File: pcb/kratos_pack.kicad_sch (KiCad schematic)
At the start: 96 parts, among them J1 USB_C_Receptacle_USB2.0, J2 PROG_CONN_STM_6p, J3 DBG_UART, J4 BAT_MID+NTC, J5 BAT_7.4V, J6 BAT_0V, J7 OUT+, J8 OUT-, Q1 AON7403, Q2 AON7414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

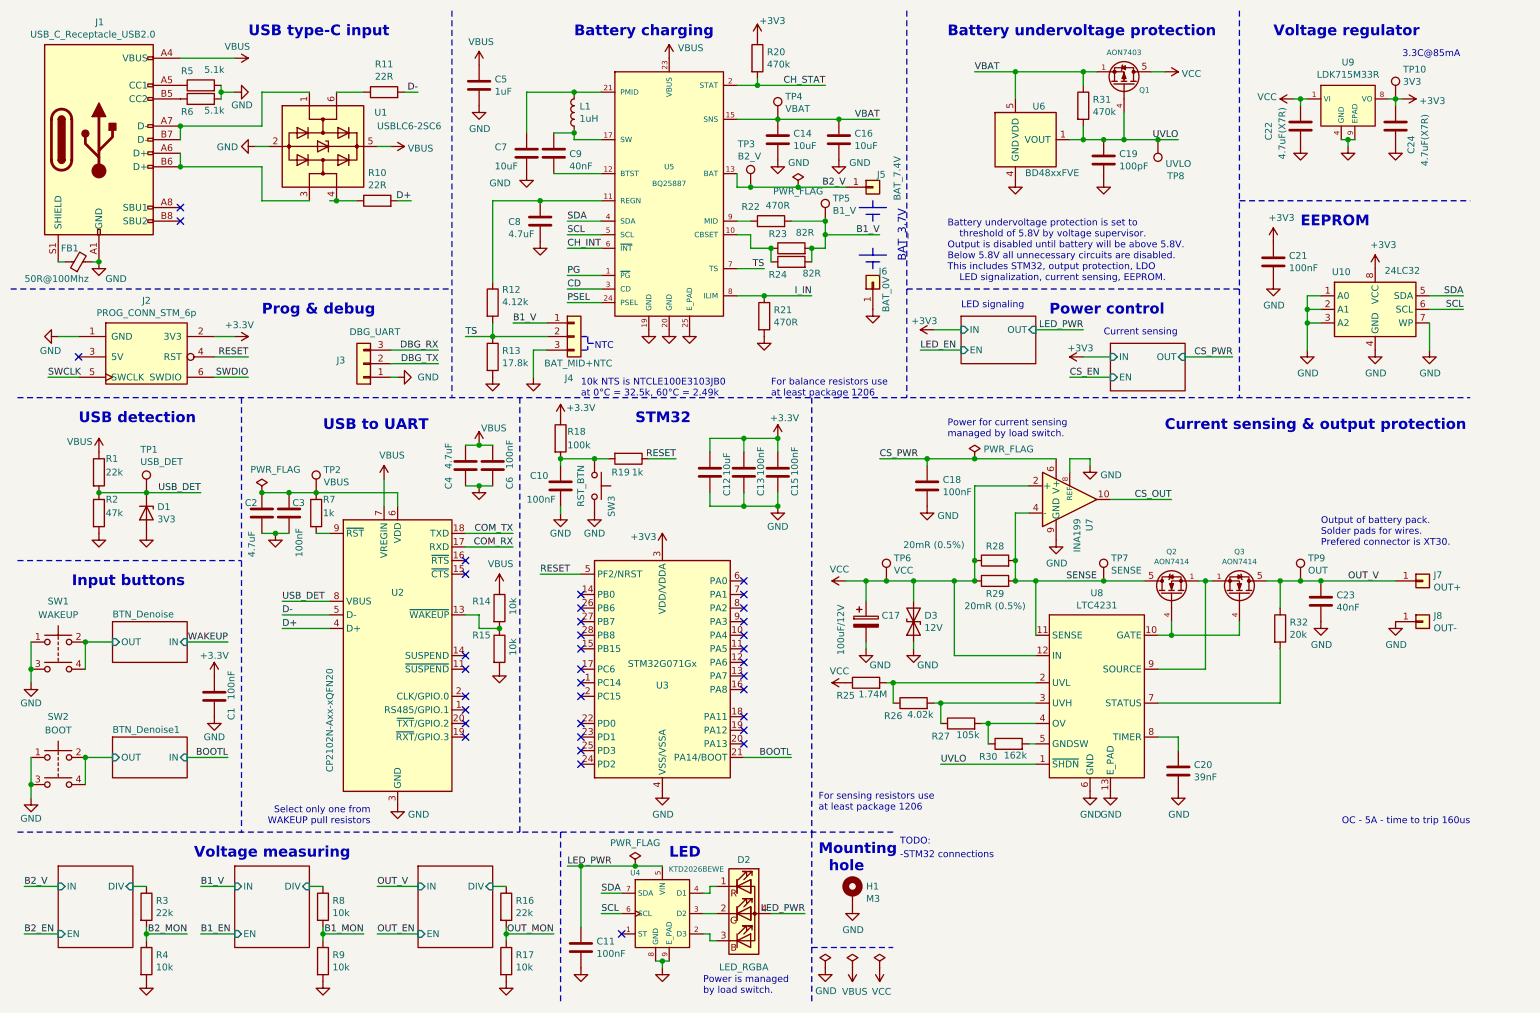
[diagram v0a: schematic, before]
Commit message: Schema: bom optimization
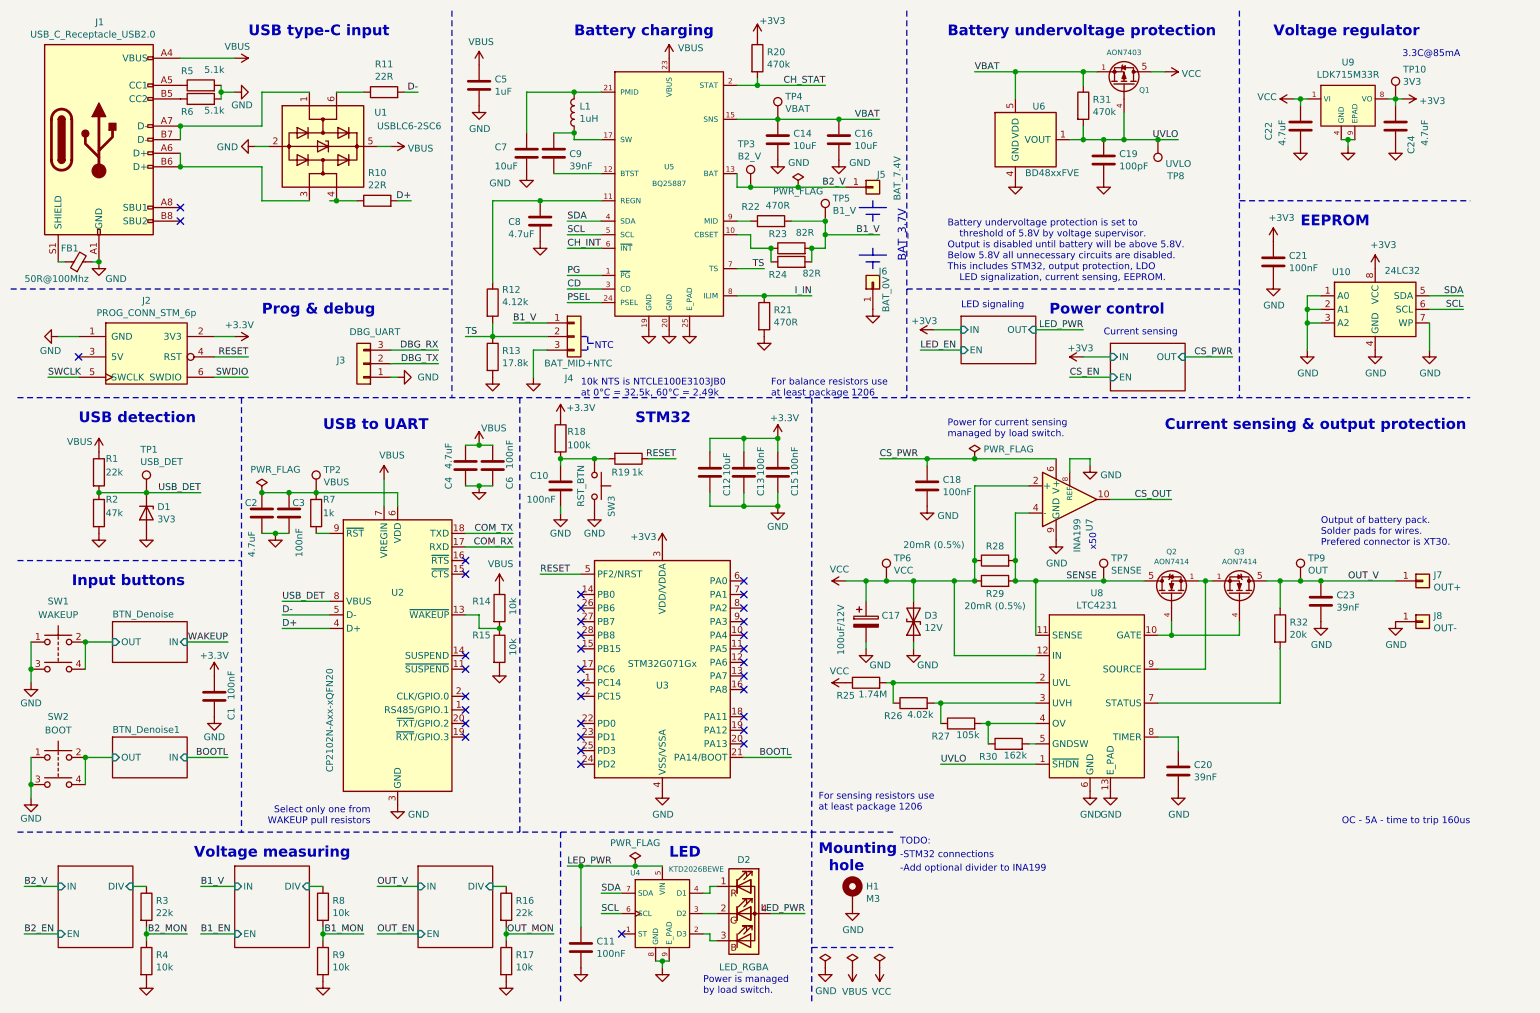
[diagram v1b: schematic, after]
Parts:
- C22, C24: value 4.7uF(X7R) -> 4.7uF
- C23, C9: value 40nF -> 39nF
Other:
- note added: "-Add optional divider to INA199"
- note added: "x50"
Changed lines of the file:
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@@
   (junction (at 261.62 36.83) (diameter 1.016) (color 0 0 0 0))
   (junction (at 270.51 29.21) (diameter 1.016) (color 0 0 0 0))
-  (no_connect (at 148.59 119.38))
-  (no_connect (at 148.59 144.78))
-  (no_connect (at 118.11 153.67))
-  (no_connect (at 118.11 148.59))
-  (no_connect (at 96.52 135.89))
-  (no_connect (at 118.11 135.89))
+  (no_connect (at 96.52 148.59))
+  (no_connect (at 118.11 121.92))
+  (no_connect (at 148.59 139.7))
   (no_connect (at 118.11 151.13))
+  (no_connect (at 96.52 133.35))
+  (no_connect (at 43.18 49.53))
+  (no_connect (at 148.59 137.16))
+  (no_connect (at 118.11 127))
+  (no_connect (at 148.59 147.32))
+  (no_connect (at 148.59 119.38))
   (no_connect (at 96.52 118.11))
-  (no_connect (at 118.11 132.08))
-  (no_connect (at 148.59 121.92))
-  (no_connect (at 118.11 129.54))
-  (no_connect (at 43.18 52.07))
-  (no_connect (at 24.13 77.47))
+  (no_connect (at 118.11 138.43))
+  (no_connect (at 118.11 148.59))
   (no_connect (at 96.52 143.51))
-  (no_connect (at 118.11 127))
-  (no_connect (at 118.11 146.05))
-  (no_connect (at 96.52 146.05))
+  (no_connect (at 148.59 121.92))
   (no_connect (at 148.59 132.08))
-  (no_connect (at 96.52 140.97))
-  (no_connect (at 148.59 147.32))
-  (no_connect (at 148.59 137.16))
-  (no_connect (at 148.59 139.7))
-  (no_connect (at 43.18 49.53))
-  (no_connect (at 148.59 124.46))
-  (no_connect (at 148.59 129.54))
-  (no_connect (at 118.11 121.92))
+  (no_connect (at 118.11 135.89))
+  (no_connect (at 96.52 146.05))
   (no_connect (at 148.59 134.62))
-  (no_connect (at 118.11 138.43))
+  (no_connect (at 148.59 144.78))
+  (no_connect (at 43.18 52.07))
+  (no_connect (at 96.52 115.57))
+  (no_connect (at 148.59 124.46))
   (no_connect (at 118.11 124.46))
-  (no_connect (at 148.59 127))
+  (no_connect (at 96.52 140.97))
   (no_connect (at 125.73 185.42))
-  (no_connect (at 96.52 115.57))
-  (no_connect (at 96.52 133.35))
-  (no_connect (at 118.11 140.97))
+  (no_connect (at 148.59 127))
+  (no_connect (at 118.11 129.54))
+  (no_connect (at 118.11 146.05))
+  (no_connect (at 24.13 77.47))
+  (no_connect (at 118.11 153.67))
   (no_connect (at 148.59 149.86))
-  (no_connect (at 96.52 148.59))
+  (no_connect (at 118.11 140.97))
+  (no_connect (at 96.52 135.89))
+  (no_connect (at 148.59 129.54))
+  (no_connect (at 118.11 132.08))
   (wire (pts (xy 13.97 176.53) (xy 20.32 176.53))
     (stroke (width 0) (type solid) (color 0 0 0 0))
@@
     (effects (font (size 1.27 1.27)) (justify left bottom))
   )
+  (text "-Add optional divider to INA199\n" (at 177.8 173.99 0)
+    (effects (font (size 1.27 1.27)) (justify left bottom))
+  )
   (text "BAT_3.7V" (at 179.07 59.69 90)
     (effects (font (size 1.5 1.5)) (justify left bottom))
@@
     (effects (font (size 2 2) (thickness 0.4) bold) (justify left bottom))
   )
+  (text "x50" (at 214.63 110.49 270)
+    (effects (font (size 1.27 1.27)) (justify right bottom))
+  )
   (text "Current sensing" (at 215.9 73.66 0)
     (effects (font (size 1.27 1.27)) (justify left bottom))
@@
   (symbol (lib_id "power:GND") (at 213.36 97.79 0) (unit 1)
     (in_bom yes) (on_board yes)
-    (property "Reference" "#PWR?" (id 0) (at 213.36 104.14 0)
+    (property "Reference" "#PWR0104" (id 0) (at 213.36 104.14 0)
       (effects (font (size 1.27 1.27)) hide)
     )
@@
       (effects (font (size 1.27 1.27)) (justify right))
     )
-    (property "Value" "40nF" (id 1) (at 115.951 41.789 0)
+    (property "Value" "39nF" (id 1) (at 115.951 41.789 0)
       (effects (font (size 1.27 1.27)) (justify right))
     )
@@
       (effects (font (size 1.27 1.27)) (justify left))
     )
-    (property "Value" "4.7uF(X7R)" (id 1) (at 249.301 40.519 90)
+    (property "Value" "4.7uF" (id 1) (at 249.301 37.979 90)
       (effects (font (size 1.27 1.27)) (justify left))
     )
@@
       (effects (font (size 1.27 1.27)) (justify left))
     )
-    (property "Value" "40nF" (id 1) (at 259.461 124.339 0)
+    (property "Value" "39nF" (id 1) (at 259.461 124.339 0)
       (effects (font (size 1.27 1.27)) (justify left))
     )
@@
       (effects (font (size 1.27 1.27)) (justify left))
     )
-    (property "Value" "4.7uF(X7R)" (id 1) (at 275.971 41.789 90)
+    (property "Value" "4.7uF" (id 1) (at 275.971 37.979 90)
       (effects (font (size 1.27 1.27)) (justify left))
     )
@@
     )
     (path "/ecc98303-85ee-40d3-ae87-d94fde20936b"
-      (reference "#PWR?") (unit 1) (value "GND") (footprint "")
+      (reference "#PWR0104") (unit 1) (value "GND") (footprint "")
     )
     (path "/d0d7f179-7f1f-4e2e-b24a-e40d8cea9459"
@@
     )
     (path "/a694cf57-5fc3-42a5-ba36-e20dd2395bd3"
-      (reference "C9") (unit 1) (value "40nF") (footprint "Capacitor_SMD:C_0603_1608Metric")
+      (reference "C9") (unit 1) (value "39nF") (footprint "Capacitor_SMD:C_0603_1608Metric")
     )
     (path "/4882b81f-66f4-4329-b7e2-48e3fe472f6d"
@@
     )
     (path "/10694819-271b-4fa5-ba61-ba7c078c1caf"
-      (reference "C22") (unit 1) (value "4.7uF(X7R)") (footprint "Capacitor_SMD:C_0603_1608Metric")
+      (reference "C22") (unit 1) (value "4.7uF") (footprint "Capacitor_SMD:C_0603_1608Metric")
     )
     (path "/bf7e2eb7-9983-4bef-ae6c-e76472d6cf02"
-      (reference "C23") (unit 1) (value "40nF") (footprint "Capacitor_SMD:C_0603_1608Metric")
+      (reference "C23") (unit 1) (value "39nF") (footprint "Capacitor_SMD:C_0603_1608Metric")
     )
     (path "/deeb4730-0fa2-42da-95d5-a11c25b6e003"
-      (reference "C24") (unit 1) (value "4.7uF(X7R)") (footprint "Capacitor_SMD:C_0603_1608Metric")
+      (reference "C24") (unit 1) (value "4.7uF") (footprint "Capacitor_SMD:C_0603_1608Metric")
     )
     (path "/9ed7c76f-3ba4-4c76-9e97-74ddd55ed5cd"

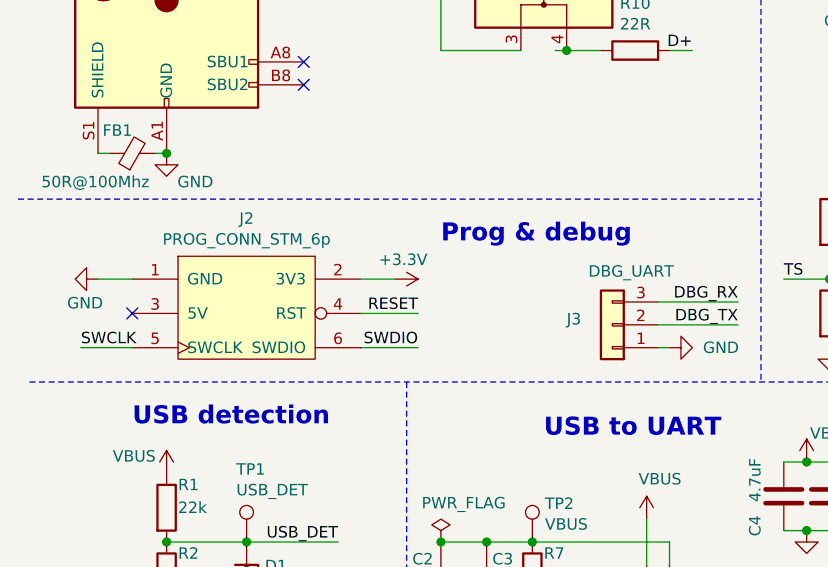
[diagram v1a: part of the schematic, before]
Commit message: Schema: update footprint 3-pin connectors, project cleanup, add gitignore
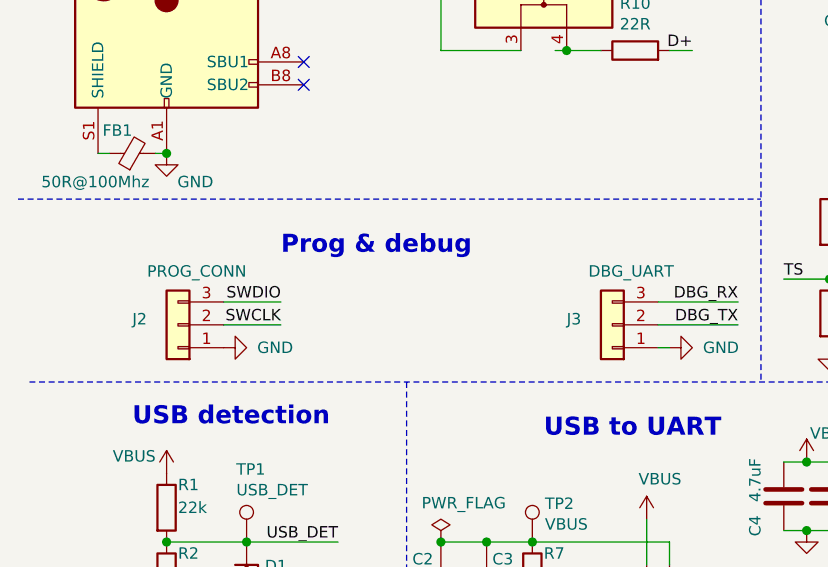
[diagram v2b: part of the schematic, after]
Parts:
- removed J2: PROG_CONN_STM_6p, Connector_PinHeader_1.27mm:PinHeader_2x03_P1.27mm_Vertical, symbol TCY_connectors:PROG_CONN_STM_6p
- added J2: PROG_CONN, TCY_connectors:Amphenol_10114828-11103LF_1x03_P1.25mm_Vertical, symbol Connector_Generic:Conn_01x03
- H1: footprint (none) -> MountingHole:MountingHole_3.2mm_M3_Pad_Via
- J3: footprint Connector_PinHeader_1.27mm:PinHeader_1x03_P1.27mm_Vertical -> TCY_connectors:Amphenol_10114828-11103LF_1x03_P1.25mm_Vertical
- J4: footprint (none) -> TCY_connectors:Amphenol_10114828-11103LF_1x03_P1.25mm_Vertical
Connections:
- net GND: now also J2.1 (Pin_1)
- net SWCLK: now also J2.2 (Pin_2)
- net SWDIO: now also J2.3 (Pin_3)
- no-connect marks 36 -> 35

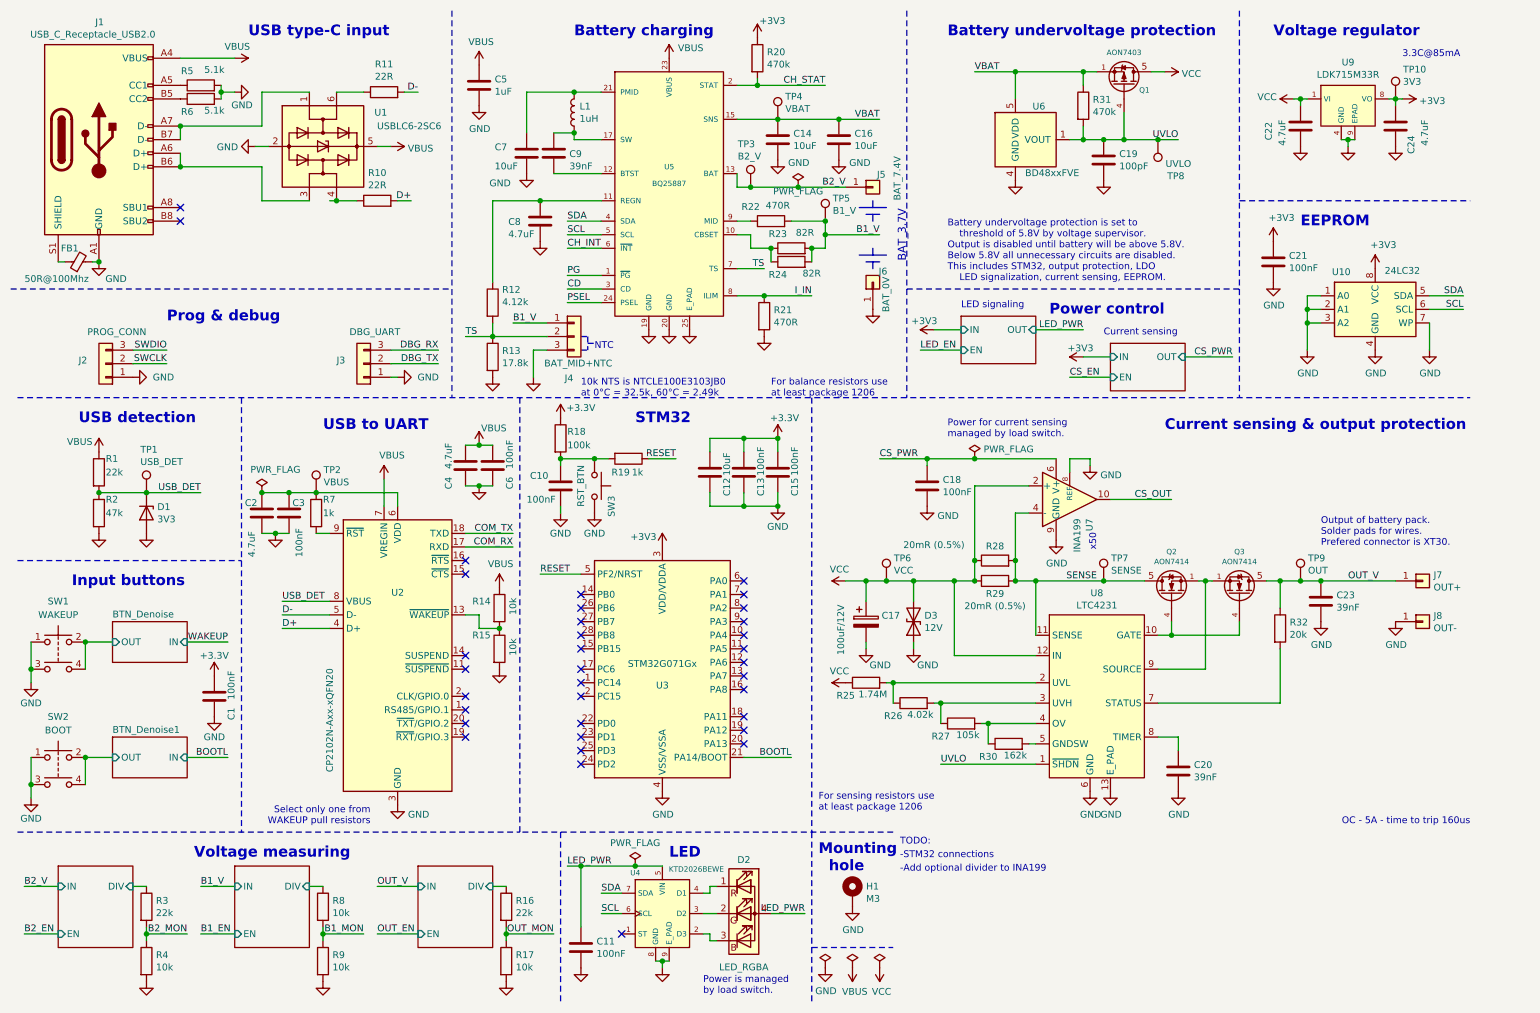
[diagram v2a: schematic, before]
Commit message: Schema: Remove unnecessary test points (switches) and filtering capacitors (STM, CP2102)
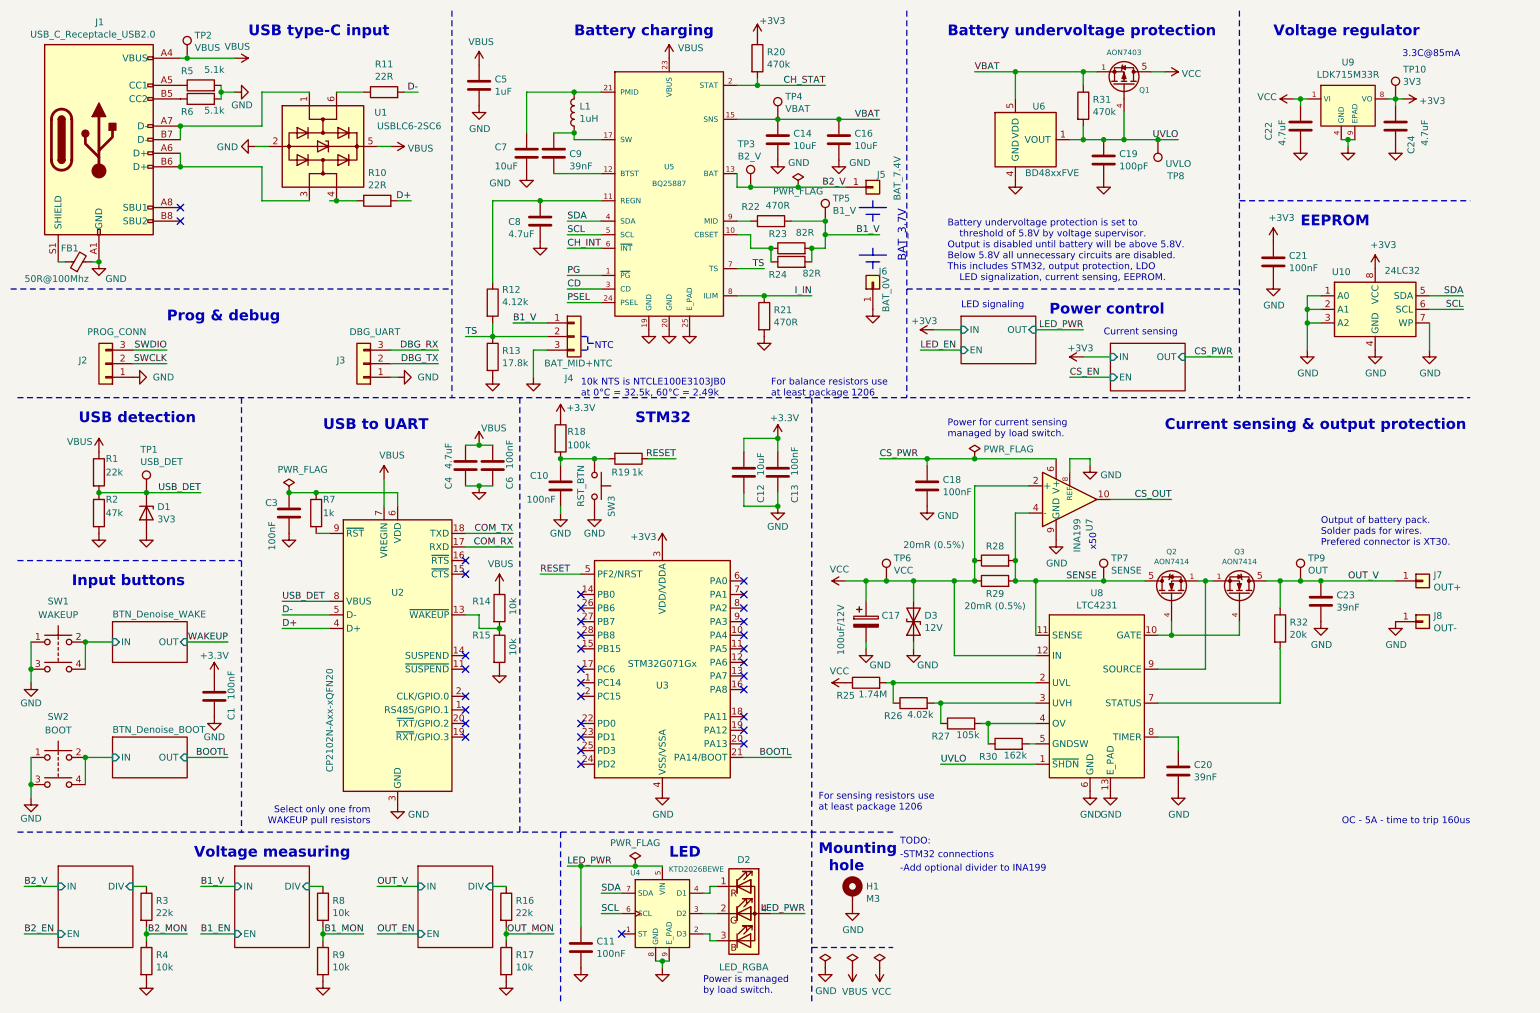
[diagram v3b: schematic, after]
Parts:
- removed C15: 100nF, Capacitor_SMD:C_0603_1608Metric, symbol Device:C
- removed C2: 4.7uF, Capacitor_SMD:C_0603_1608Metric, symbol Device:C
- TP1, TP10, TP2, TP3, TP4, TP5, TP6, TP7, TP8, TP9: footprint TestPoint:TestPoint_Pad_D1.0mm -> TCY_connectors:TestPoint_Pad_D0.5mm
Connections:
- net VBUS: now also TP2.1
- net at C3.1, R7.1, U2.6 (VDD): no longer TP2.1
- net BTN_Denoise_WAKE/OUT renamed BTN_Denoise_WAKE/IN
- net BTN_Denoise_BOOT/OUT renamed BTN_Denoise_BOOT/IN
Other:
- sheet BTN_Denoise renamed BTN_Denoise_WAKE
- sheet BTN_Denoise1 renamed BTN_Denoise_BOOT
- moved on the sheet: C12, C13, TP2
